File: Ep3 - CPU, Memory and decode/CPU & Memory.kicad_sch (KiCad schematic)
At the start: 16 parts, among them U10 AS6C4008, U11 ATF22V10C-7, U5 74HCT132, U7 74HCT32, U8 SST39SF010, U9 ATF22V10C-7

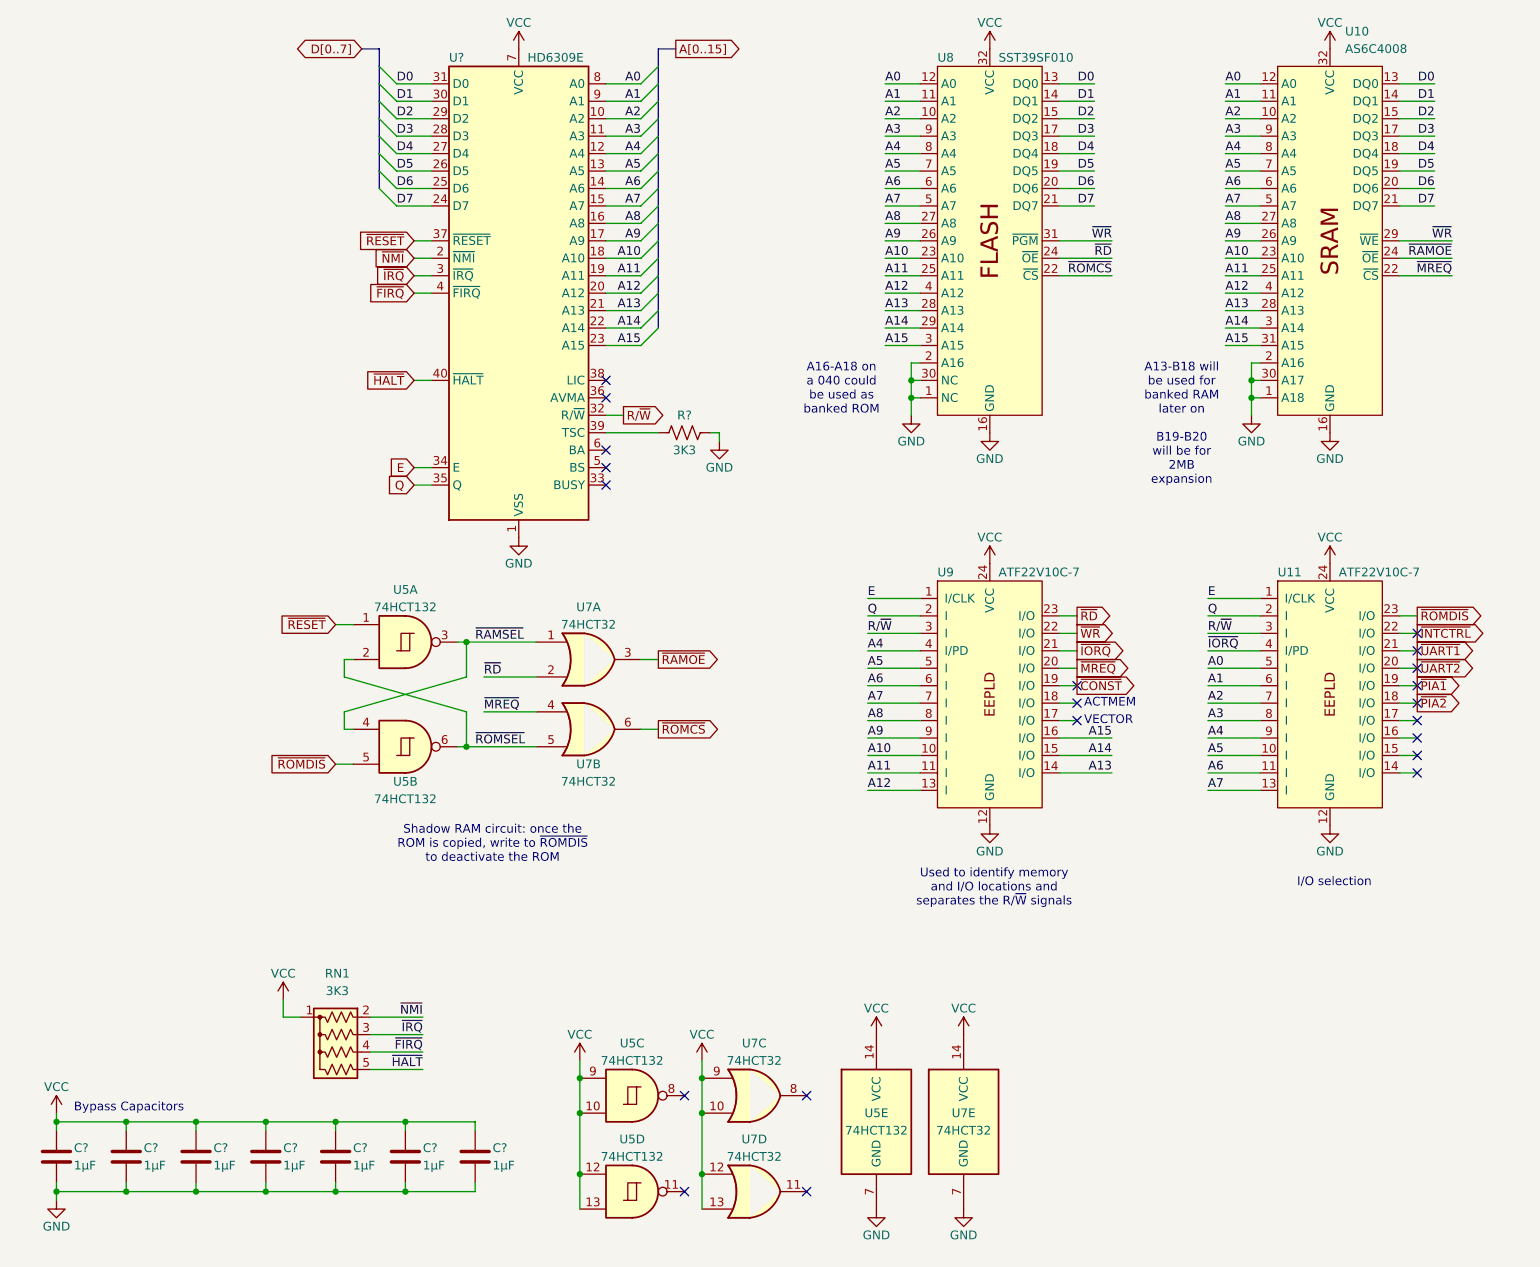
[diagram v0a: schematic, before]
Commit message: Minor cosmetic changes
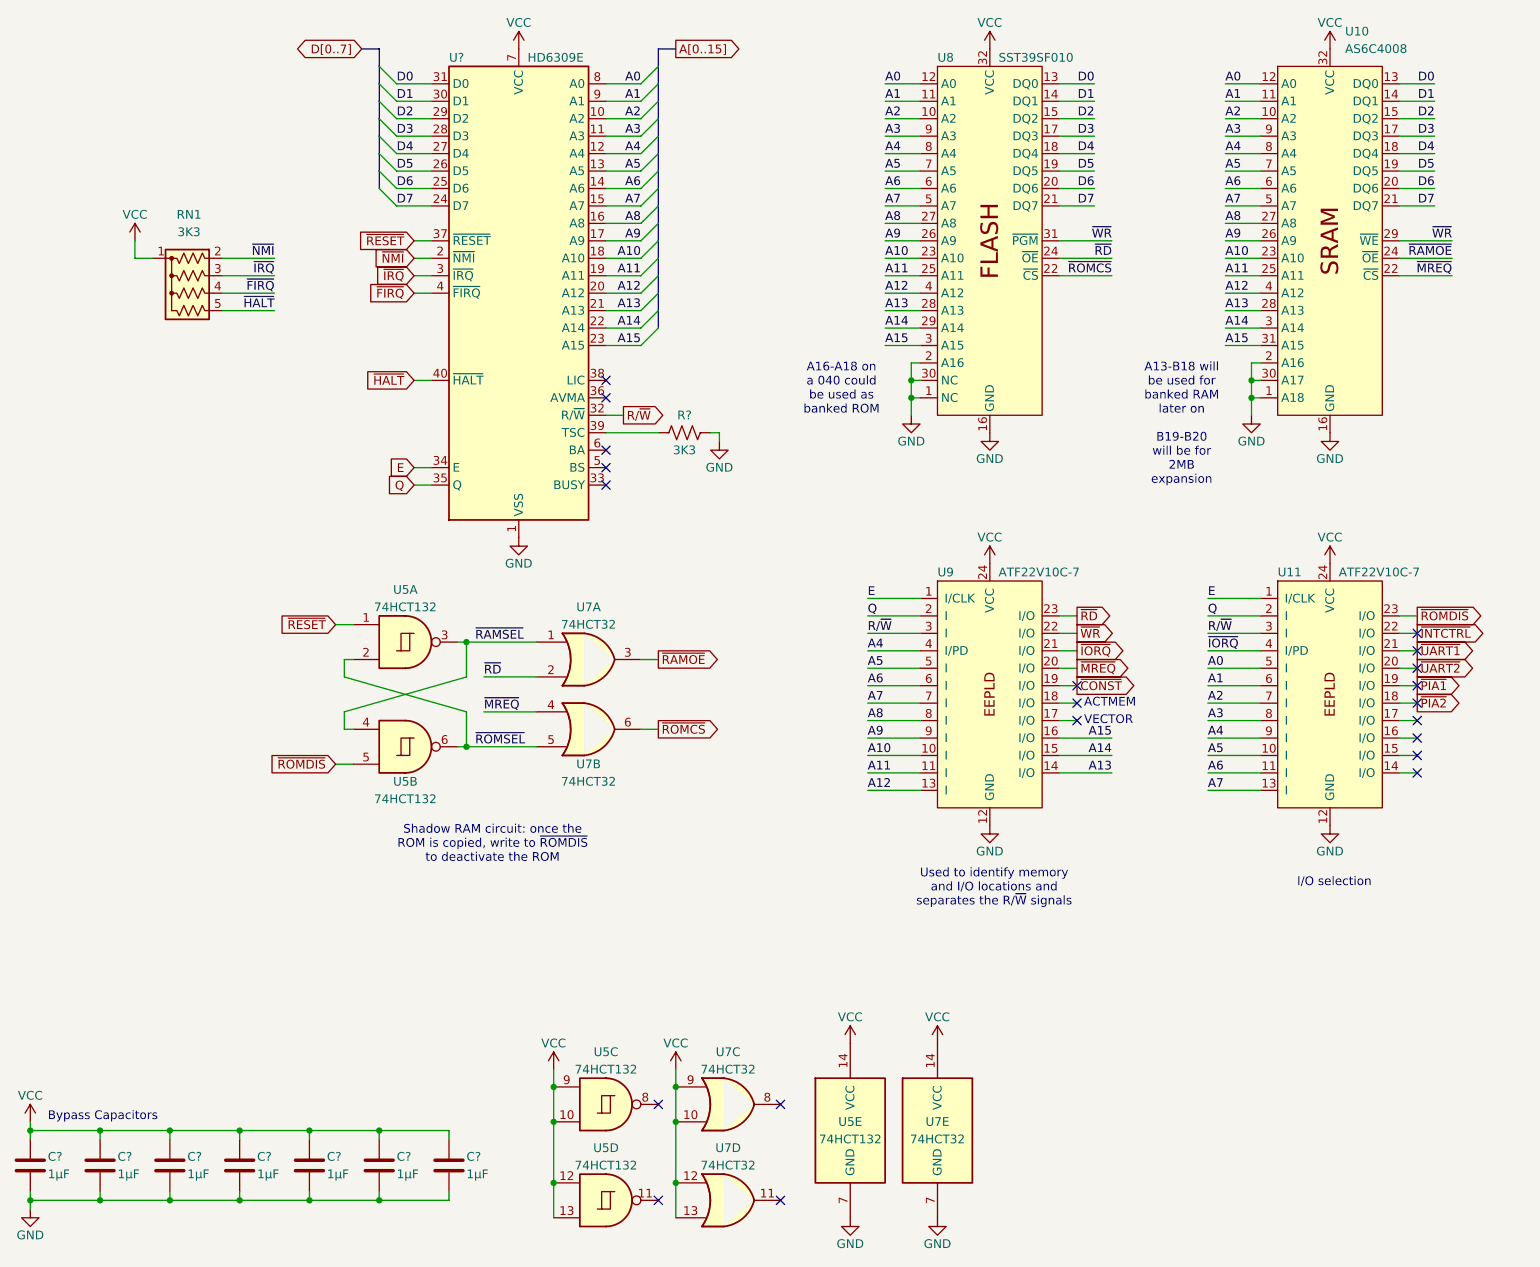
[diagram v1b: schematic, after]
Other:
- moved on the sheet: C?, RN1, U5C, U5D, U5E, U7C, U7D, U7E
